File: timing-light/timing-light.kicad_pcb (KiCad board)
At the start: 2 copper layers, 35 parts, among them J1 Conn_01x02_Male, J2 Conn_01x02_Female, Q1 IRFB3004PbF, Q2 IRFB3004PbF, U1 4001

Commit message: [timing-light] update
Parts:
- moved J_light2 148.7 mm to (113.0, 68.6), turned to 180 degrees
- moved J_light1 108.6 mm to (69.8, 137.2)
- moved U_dr1 96.7 mm to (72.4, 115.6)
- moved C_u_dr1 95.0 mm to (74.9, 96.5)
- moved D3 41.4 mm to (121.9, 77.5), turned to 180 degrees
- moved Q2 33.7 mm to (101.1, 50.8), turned to -90 degrees
- moved R_light1 24.3 mm to (96.5, 64.8)
- moved D4 23.3 mm to (100.3, 77.5)
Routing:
- net +12V: track 11.1 -> 104.7 mm
- net Net-(D3-Pad2): track 0.00 -> 40.2 mm
- net GND: track 63.1 -> 102.9 mm
- net Net-(J_light1-Pad1): track 0.00 -> 12.4 mm
- net Net-(J_light1-Pad2): track 0.00 -> 11.6 mm
- net Net-(Q2-Pad3): track 0.00 -> 9.09 mm
- net /on_off_dr: track 0.00 -> 6.87 mm

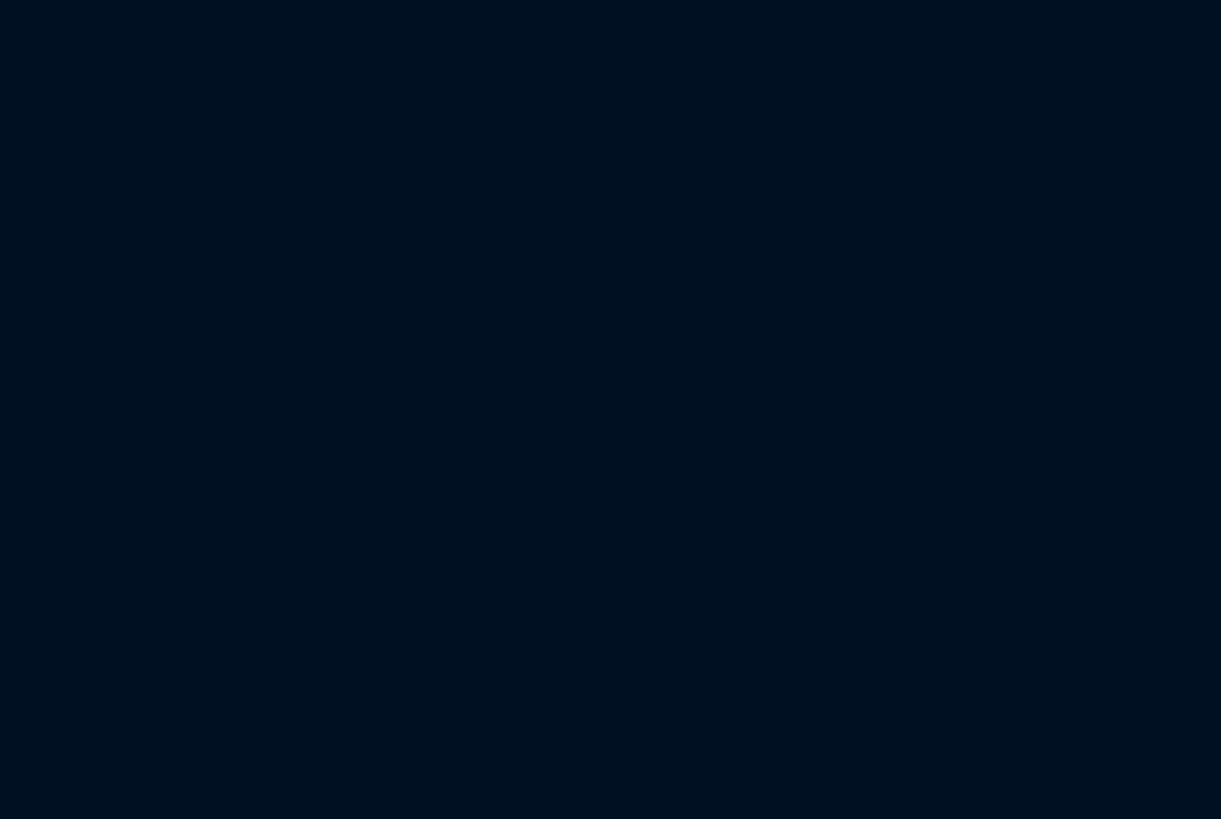
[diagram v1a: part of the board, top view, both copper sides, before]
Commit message: [timing-light] Use BU941ZP as ignition coil driver
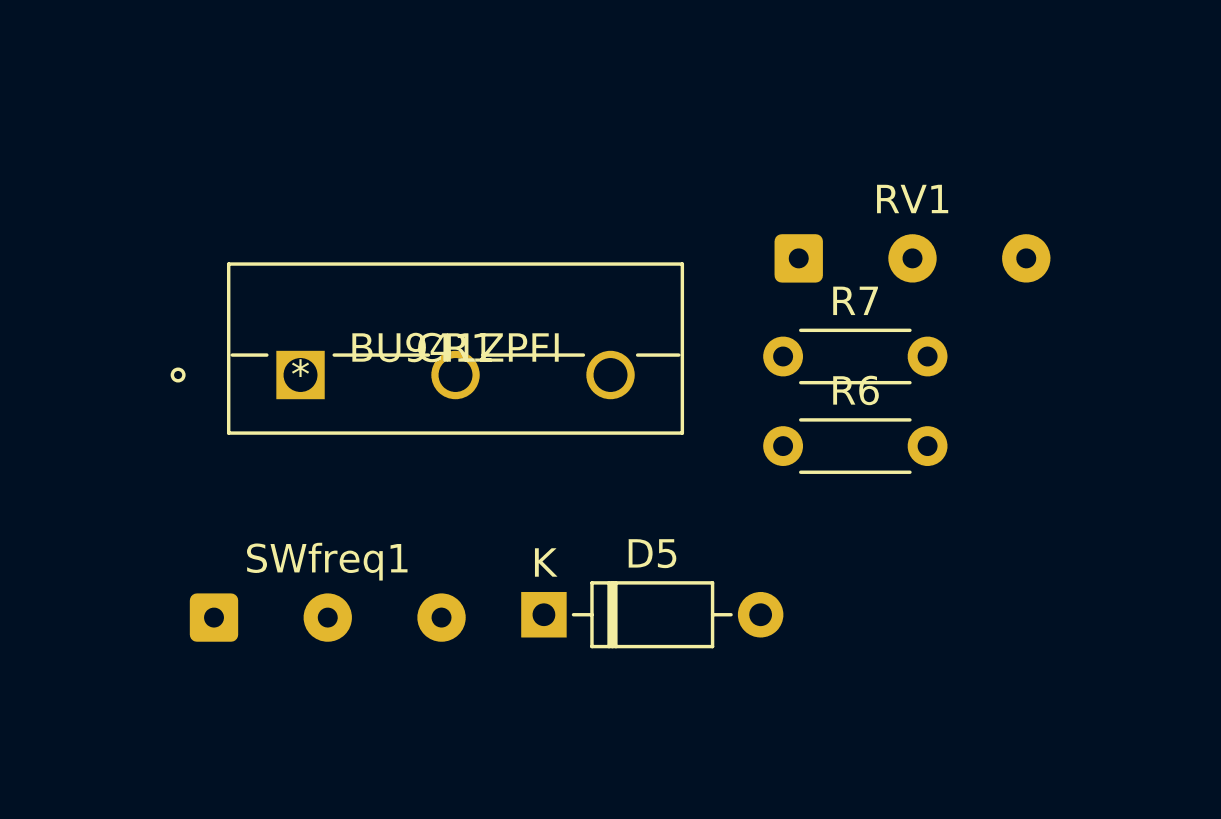
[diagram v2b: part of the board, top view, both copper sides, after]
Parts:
- added CR1: BU941ZPFI, LIB:BU941ZPFI, F.Cu at (167.6, 77.5)
- added D5: BAT42, Diode_THT:D_DO-35_SOD27_P7.62mm_Horizontal, F.Cu at (176.2, 85.9)
- added R6: 1k, Resistor_THT:R_Axial_DIN0204_L3.6mm_D1.6mm_P5.08mm_Horizontal, F.Cu at (184.6, 80.0)
- added R7: 1k, Resistor_THT:R_Axial_DIN0204_L3.6mm_D1.6mm_P5.08mm_Horizontal, F.Cu at (184.6, 76.8)
- added RV1: 470k, Connector_Wire:SolderWire-0.15sqmm_1x03_P4mm_D0.5mm_OD1.5mm, F.Cu at (185.2, 73.4)
- added SWfreq1: SW_SPDT, Connector_Wire:SolderWire-0.15sqmm_1x03_P4mm_D0.5mm_OD1.5mm, F.Cu at (164.6, 86.0)
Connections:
- D1 pad 2: Net-(D1-Pad2) -> Net-(CR1-Pad2)
- D2 pad 1: Net-(D1-Pad2) -> Net-(CR1-Pad2)
- J2 pad 2: Net-(J2-Pad2) -> Net-(CR1-Pad1)
- J_coil1 pad 2: Net-(D1-Pad2) -> Net-(CR1-Pad2)
- R5 pad 2: Net-(R5-Pad2) -> Net-(D5-Pad2)
- TP1 pad 1: Net-(R5-Pad2) -> Net-(D5-Pad2)
- U_ign1 pad 2: /U_ign_tr -> /Uign_trig
- U_ign1 pad 3: Net-(R5-Pad2) -> Net-(D5-Pad2)
- U_ign1 pad 5: (no net) -> unconnected-(U_ign1-Pad5)
- U_ign1 pad 6: /U_ign_tr -> /Uign_trig
- U_ign1 pad 7: (no net) -> /Uign_dis
